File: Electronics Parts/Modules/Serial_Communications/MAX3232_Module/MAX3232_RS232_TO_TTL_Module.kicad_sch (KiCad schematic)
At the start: 18 parts, among them U1 MAX3232

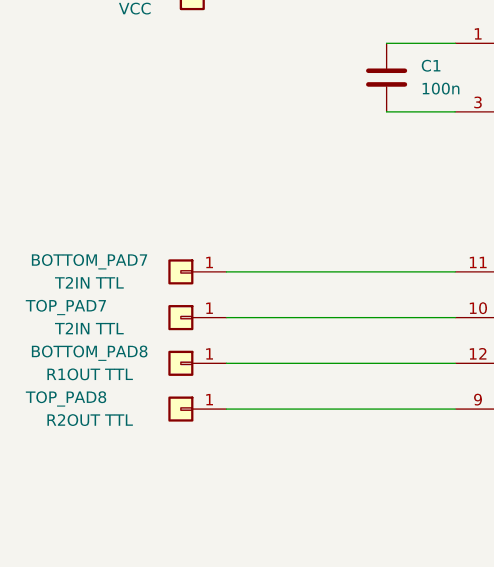
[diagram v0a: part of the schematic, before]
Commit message: Kicad max3232 (#3)
* Update Serial_Communications directory

Add the KiCad schematic for the MAX3232 Module
Update the Max3232_Module.
Add the schematic and label document for a MAX3232 Breadboard module
Add the schematic for the MH_TTL-RS232_Bidirectional converter
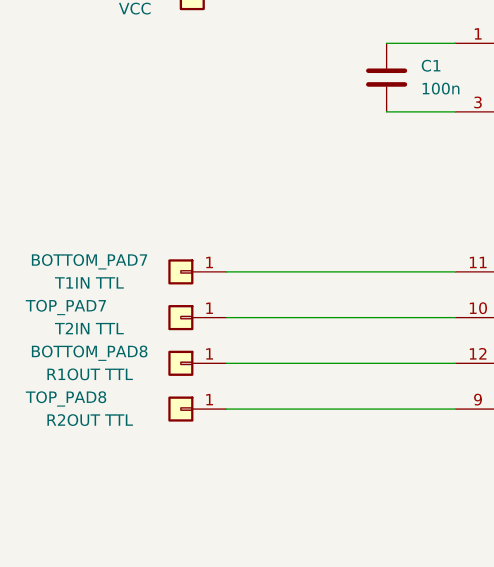
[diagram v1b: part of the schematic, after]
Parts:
- BOTTOM_PAD7: value T2IN TTL -> T1IN TTL
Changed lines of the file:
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@@
     (in_bom yes) (on_board yes)
     (property "Reference" "BOTTOM_PAD7" (id 0) (at 86.36 86.36 0))
-    (property "Value" "T2IN TTL" (id 1) (at 86.36 88.9 0))
+    (property "Value" "T1IN TTL" (id 1) (at 86.36 88.9 0))
     (property "Footprint" "" (id 2) (at 96.52 87.63 0)
       (effects (font (size 1.27 1.27)) hide)
@@
     )
     (path "/f6bc4b0a-2446-412c-bdef-2aed77bef9ef"
-      (reference "BOTTOM_PAD7") (unit 1) (value "T2IN TTL") (footprint "")
+      (reference "BOTTOM_PAD7") (unit 1) (value "T1IN TTL") (footprint "")
     )
     (path "/e8b1b24d-8a70-435d-ba02-786aaad18b3d"
